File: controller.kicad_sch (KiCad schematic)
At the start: 40 parts, among them U1 TMC4671, U2 74LVC3G17, U3 74LVC3G17

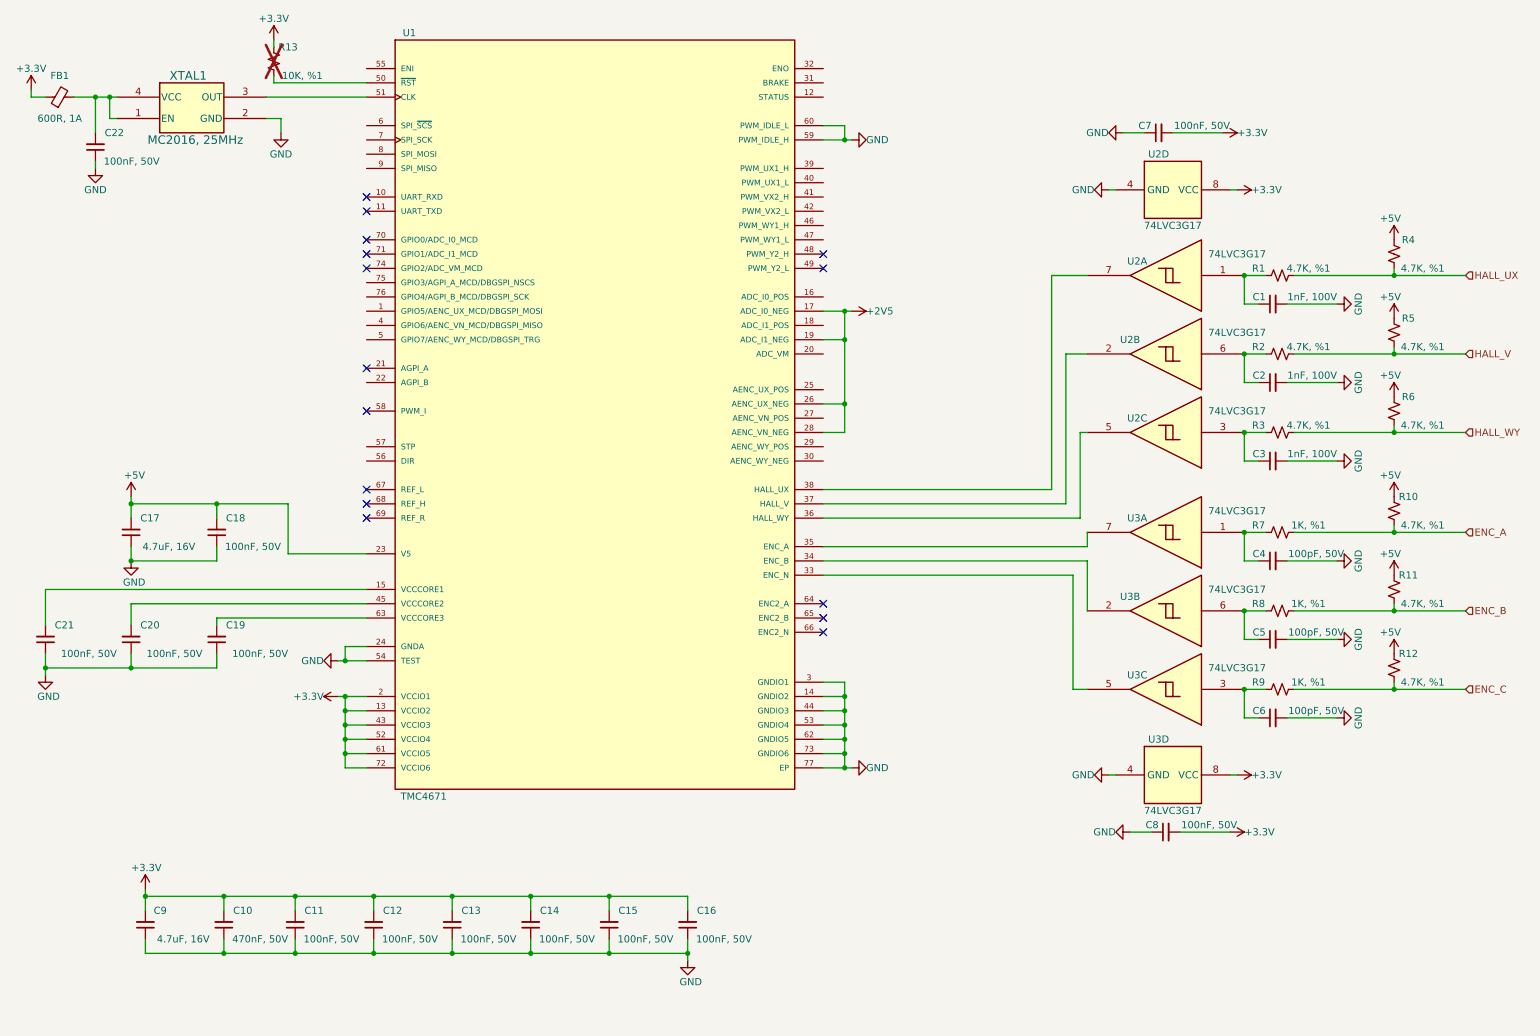
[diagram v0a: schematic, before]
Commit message: Finish controller and driver schematics.
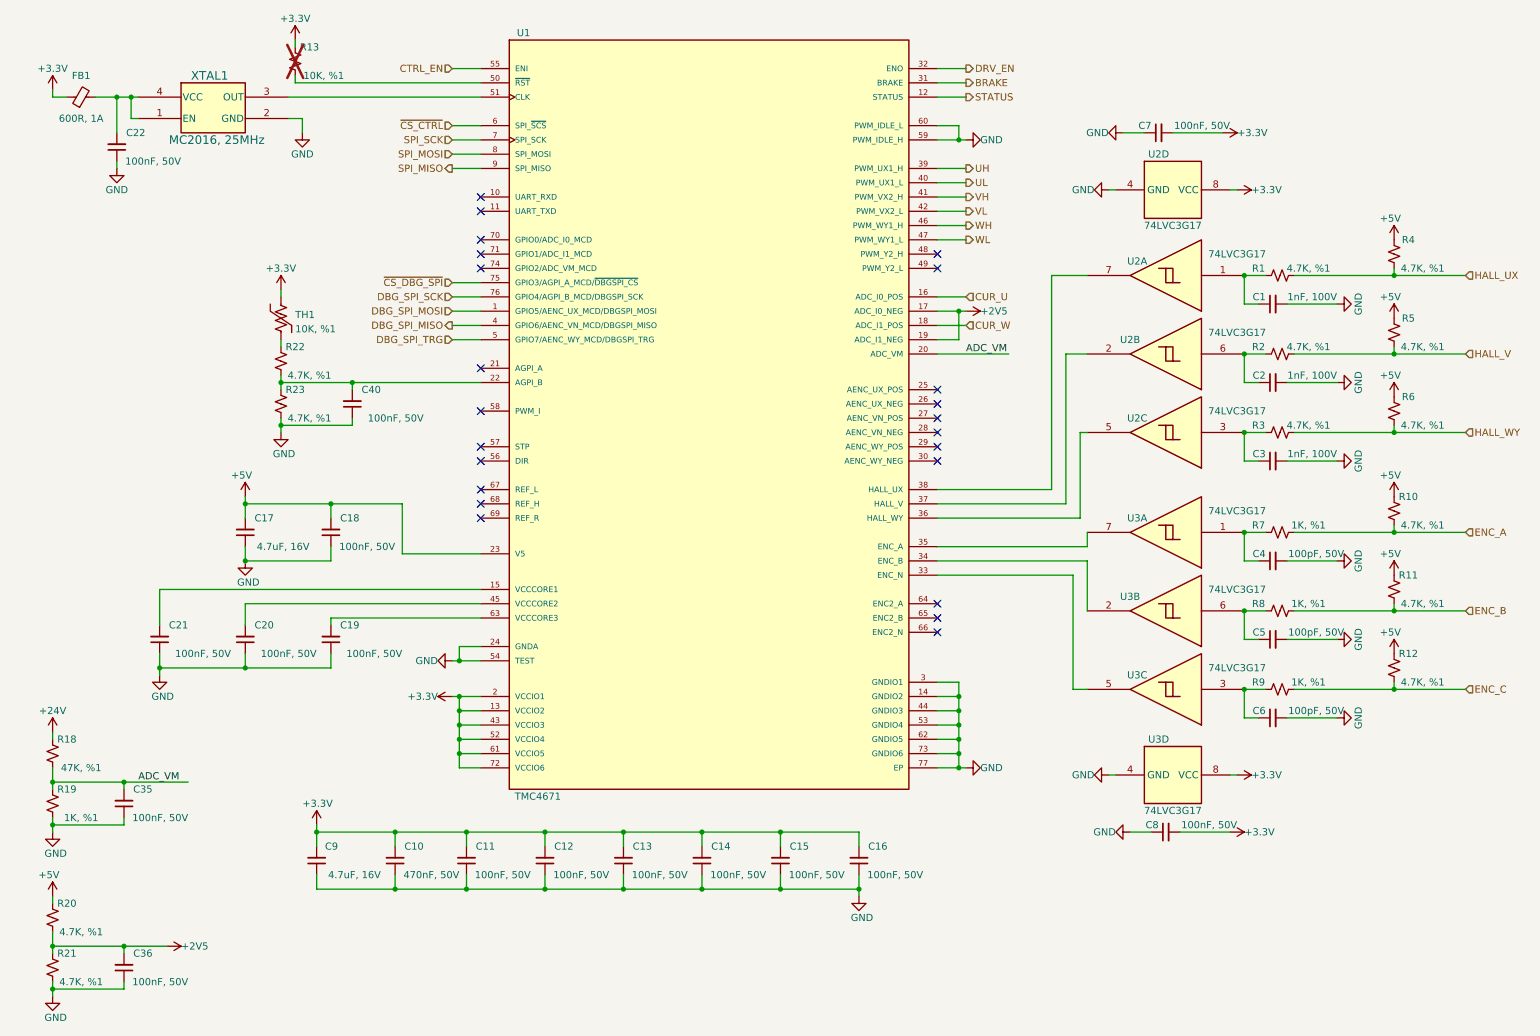
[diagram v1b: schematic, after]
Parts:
- added C35, C36, C40: 100nF, 50V, symbol Device:C_Small
- added R18: 47K, %1, symbol Device:R_Small_US
- added R19: 1K, %1, symbol Device:R_Small_US
- added R20, R21, R22, R23: 4.7K, %1, symbol Device:R_Small_US
- added TH1: 10K, %1, symbol Device:Thermistor_US
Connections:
- net +2V5: now also C36.2, R20.1, R21.2; no longer U1.26 (AENC_UX_NEG), U1.28 (AENC_VN_NEG)
- net +3.3V: now also TH1.1
- net +5V: now also R20.2
- net GND: now also C35.1, C36.1, C40.1, R19.1, R21.1, R23.1
- net DBG_SPI_MOSI: now reaches U1.1 (GPIO5/AENC_UX_MCD/DBGSPI_MOSI)
- net STATUS: now reaches U1.12 (STATUS)
- net CUR_U: now reaches U1.16 (ADC_I0_POS)
- net CUR_W: now reaches U1.18 (ADC_I1_POS)
- net ADC_VM: now reaches U1.20 (ADC_VM)
- net ADC_VM: now also C35.2, R18.1, R19.2
- net at U1.22 (AGPI_B): now also C40.2, R22.1, R23.2
- net BRAKE: now reaches U1.31 (BRAKE)
- net DRV_EN: now reaches U1.32 (ENO)
- net UH: now reaches U1.39 (PWM_UX1_H)
- net DBG_SPI_MISO: now reaches U1.4 (GPIO6/AENC_VN_MCD/DBGSPI_MISO)
- net UL: now reaches U1.40 (PWM_UX1_L)
- net VH: now reaches U1.41 (PWM_VX2_H)
- net VL: now reaches U1.42 (PWM_VX2_L)
- net WH: now reaches U1.46 (PWM_WY1_H)
- net WL: now reaches U1.47 (PWM_WY1_L)
- net DBG_SPI_TRG: now reaches U1.5 (GPIO7/AENC_WY_MCD/DBGSPI_TRG)
- net CTRL_EN: now reaches U1.55 (ENI)
- net ~{CS_CTRL}: now reaches U1.6 (SPI_~{SCS})
- net SPI_SCK: now reaches U1.7 (SPI_SCK)
- net ~{CS_DBG_SPI}: now reaches U1.75 (GPIO3/AGPI_A_MCD/~{DBGSPI_CS})
- net DBG_SPI_SCK: now reaches U1.76 (GPIO4/AGPI_B_MCD/DBGSPI_SCK)
- net SPI_MOSI: now reaches U1.8 (SPI_MOSI)
- net SPI_MISO: now reaches U1.9 (SPI_MISO)
- new net: R22.2, TH1.2
- new net +24V: R18.2
- no-connect marks 15 -> 23
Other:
- moved on the sheet: C10, C11, C12, C13, C14, C15, C16, C17, C18, C19, C20, C21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

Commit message: Assign footprints and part numbers.
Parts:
- C1, C2, C3: footprint (none) -> Capacitor_SMD:C_0603_1608Metric; MPN (none) -> C0603C102K1RAC7867
- C10: footprint (none) -> Capacitor_SMD:C_0603_1608Metric; MPN (none) -> C1608X7R1H474K080AC
- C11, C12, C13, C14, C15, C16, C18, C19, C20, C21, C22, C35, C36, C40, C7, C8: footprint (none) -> Capacitor_SMD:C_0603_1608Metric; MPN (none) -> C0603C103K5RAC7867
- C17, C9: footprint (none) -> Capacitor_SMD:C_0805_2012Metric; MPN (none) -> C0805C475K4RAC7800
- C4, C5, C6: footprint (none) -> Capacitor_SMD:C_0603_1608Metric; MPN (none) -> C0603C101K5RAC7867
- FB1: footprint (none) -> Resistor_SMD:R_0603_1608Metric
- R1, R10, R11, R12, R2, R20, R21, R22, R23, R3, R4, R5, R6: footprint (none) -> Resistor_SMD:R_0603_1608Metric; MPN (none) -> ERJ-3EKF4701V
- R13, TH1: footprint (none) -> Resistor_SMD:R_0603_1608Metric; MPN (none) -> NCP18XH103F03RB
- R18: footprint (none) -> Resistor_SMD:R_0603_1608Metric; MPN (none) -> ERJ-3EKF4702V
- R19, R7, R8, R9: footprint (none) -> Resistor_SMD:R_0603_1608Metric; MPN (none) -> ERJ-3EKF1001V
- U1: MPN (none) -> TMC4671-LA
- U2, U3: footprint (none) -> Package_SO:VSSOP-8_2.3x2mm_P0.5mm; MPN (none) -> 74LVC3G17DC,125

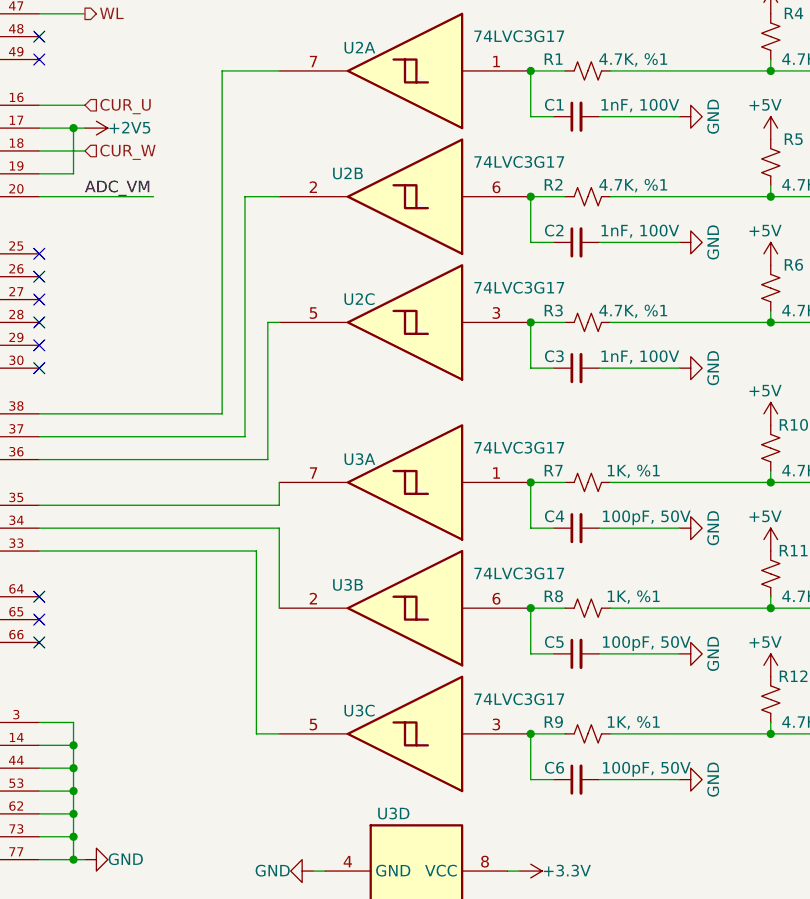
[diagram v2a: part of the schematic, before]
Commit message: Finish the initial placement, switch most of the parts to 0402.
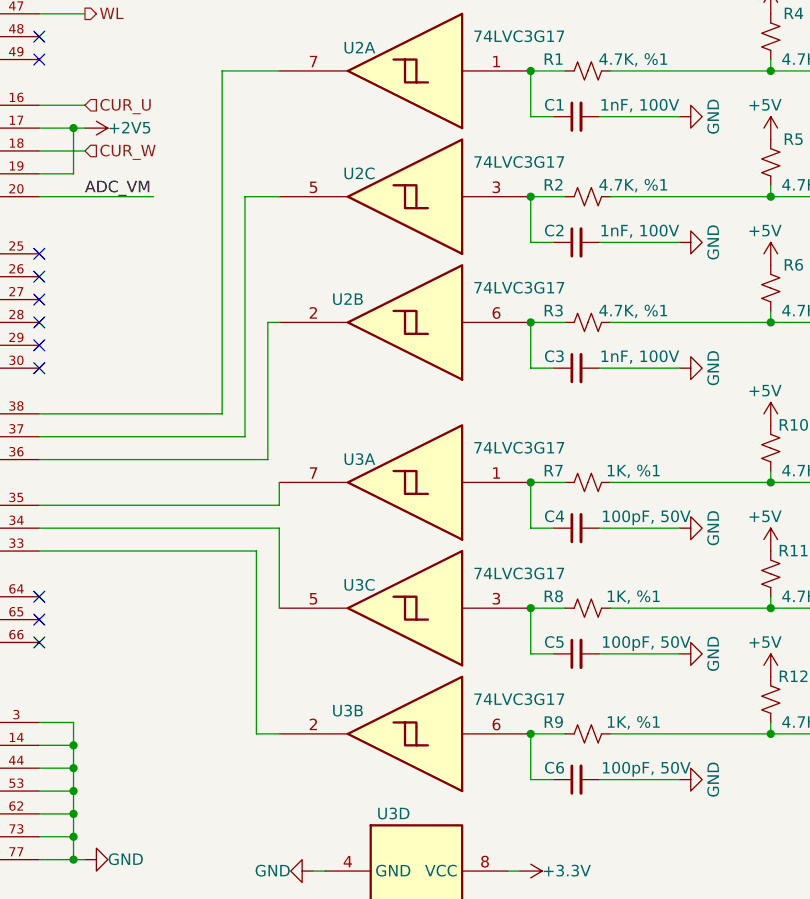
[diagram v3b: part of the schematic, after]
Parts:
- C1, C2, C3: footprint Capacitor_SMD:C_0603_1608Metric -> Capacitor_SMD:C_0402_1005Metric; MPN C0603C102K1RAC7867 -> 885012205080
- C11, C12, C13, C14, C15, C16, C18, C19, C20, C21, C22, C35, C36, C40, C7, C8: footprint Capacitor_SMD:C_0603_1608Metric -> Capacitor_SMD:C_0402_1005Metric; MPN C0603C103K5RAC7867 -> CL05B104KB54PNC
- C17, C9: footprint Capacitor_SMD:C_0805_2012Metric -> Capacitor_SMD:C_0603_1608Metric; MPN C0805C475K4RAC7800 -> GRM188Z71C475KE21J
- C4, C5, C6: footprint Capacitor_SMD:C_0603_1608Metric -> Capacitor_SMD:C_0402_1005Metric; MPN C0603C101K5RAC7867 -> 885012205055
- R1, R10, R11, R12, R2, R20, R21, R22, R23, R3, R4, R5, R6: footprint Resistor_SMD:R_0603_1608Metric -> Resistor_SMD:R_0402_1005Metric; MPN ERJ-3EKF4701V -> ERJ-2RKF4701X
- R13: footprint Resistor_SMD:R_0603_1608Metric -> Resistor_SMD:R_0402_1005Metric; MPN NCP18XH103F03RB -> RC1005F103CS
- R18: footprint Resistor_SMD:R_0603_1608Metric -> Resistor_SMD:R_0402_1005Metric; MPN ERJ-3EKF4702V -> ERJ-2RKF4702X
- R19, R7, R8, R9: footprint Resistor_SMD:R_0603_1608Metric -> Resistor_SMD:R_0402_1005Metric; MPN ERJ-3EKF1001V -> ERJ-2RKF1001X
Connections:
- net at C2.1, R2.1: now also U2.3; no longer U2.6
- net at C5.1, R8.1: now also U3.3; no longer U3.6
- net at U1.33 (ENC_N): now also U3.2; no longer U3.5
- net at U1.34 (ENC_B): now also U3.5; no longer U3.2
- net at U1.36 (HALL_WY): now also U2.2; no longer U2.5
- net at U1.37 (HALL_V): now also U2.5; no longer U2.2
- net at C6.1, R9.1: now also U3.6; no longer U3.3
- net at C3.1, R3.1: now also U2.6; no longer U2.3

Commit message: Cleanup part properties.
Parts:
- U1: MANUFACTURER Trinamic Motion -> (none); MAXIMUM_PACKAGE_HEIGHT 0.9mm -> (none); PARTREV V1.06 -> (none); STANDARD IPC 7351B -> (none)
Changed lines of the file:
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@@
       (effects (font (size 1.27 1.27)) hide)
-    )
-    (property "MAXIMUM_PACKAGE_HEIGHT" "0.9mm" (at 137.16 92.71 0)
-      (effects (font (size 1.27 1.27)) (justify bottom) hide)
-    )
-    (property "MANUFACTURER" "Trinamic Motion" (at 137.16 92.71 0)
-      (effects (font (size 1.27 1.27)) (justify bottom) hide)
-    )
-    (property "PARTREV" "V1.06" (at 137.16 92.71 0)
-      (effects (font (size 1.27 1.27)) (justify bottom) hide)
-    )
-    (property "STANDARD" "IPC 7351B" (at 137.16 92.71 0)
-      (effects (font (size 1.27 1.27)) (justify bottom) hide)
     )
     (property "MPN" "TMC4671-LA" (at 137.16 92.71 0)

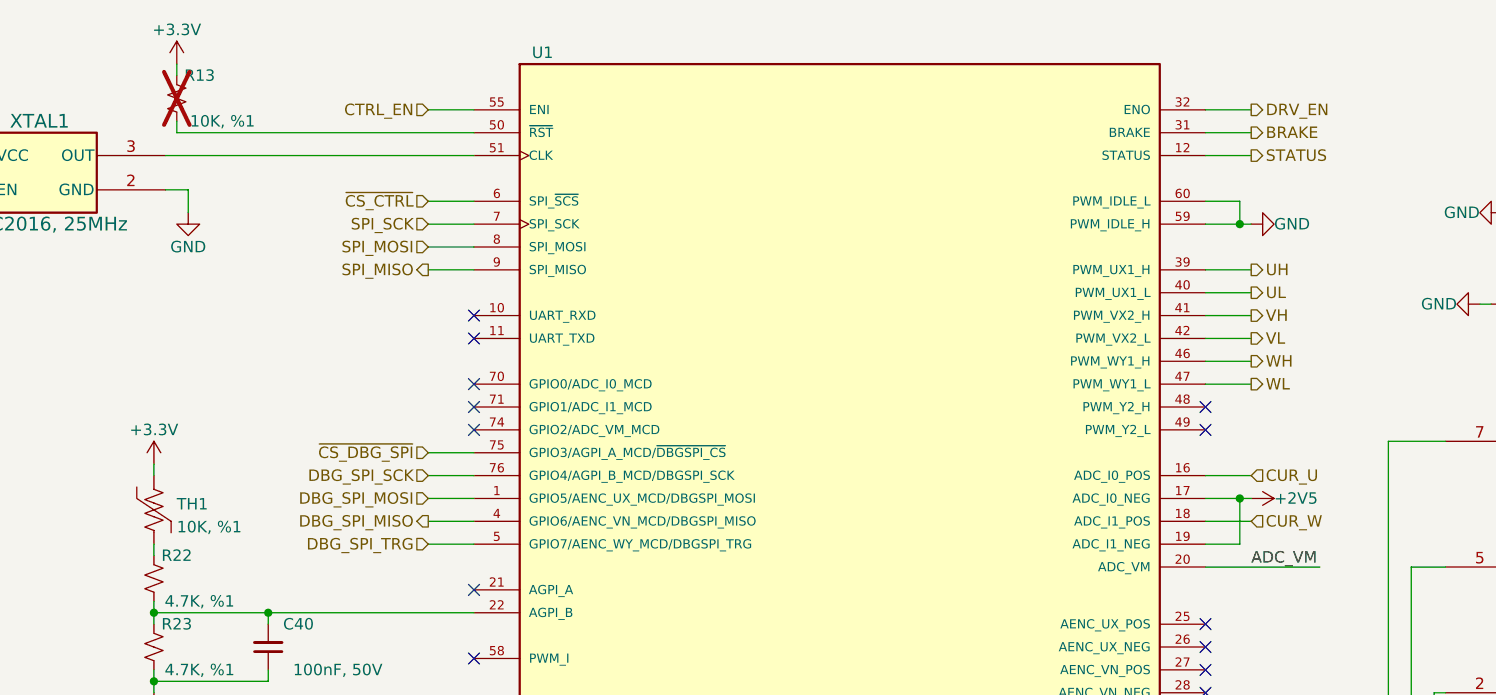
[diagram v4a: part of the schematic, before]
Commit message: Fix issues found during the test, in the schematics.
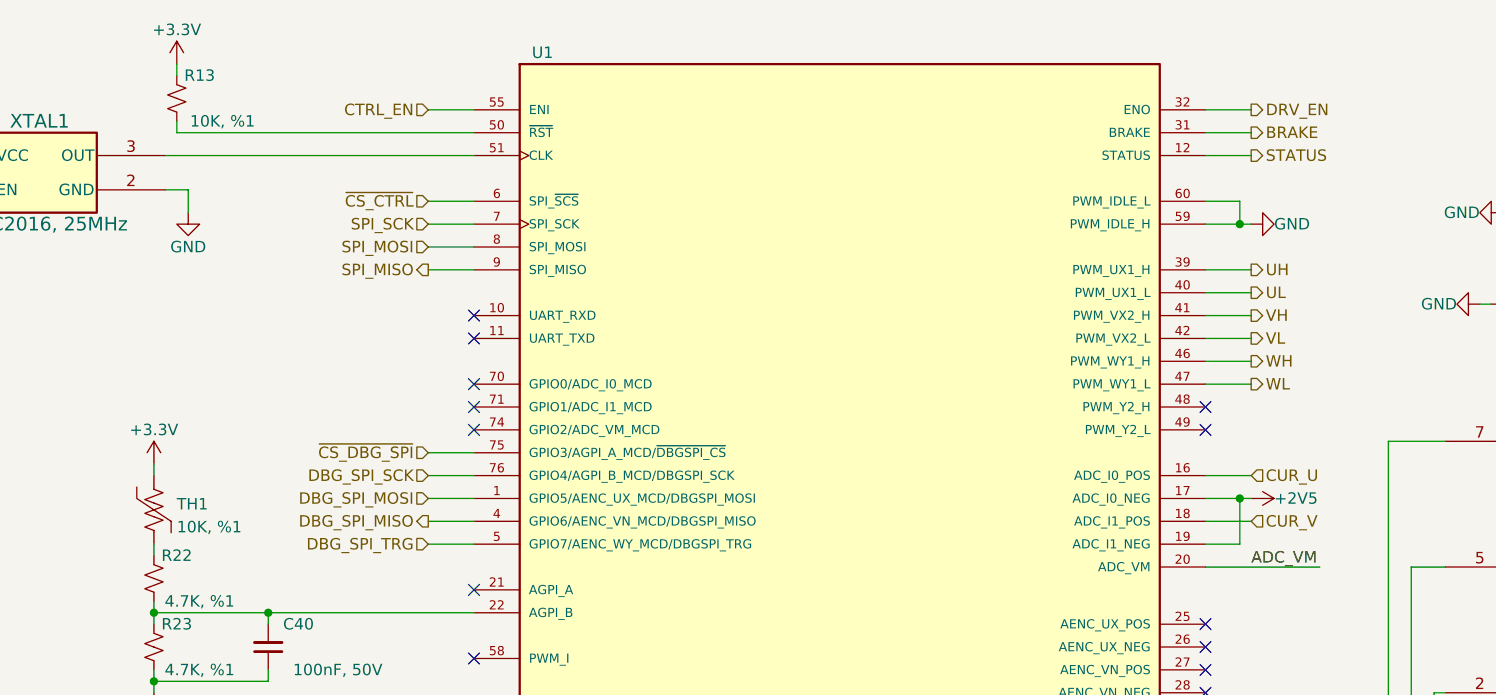
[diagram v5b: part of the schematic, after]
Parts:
- R13: now fitted
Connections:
- net CUR_W renamed CUR_V
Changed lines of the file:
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@@
     (effects (font (size 1.27 1.27)) (justify left))
   )
-  (hierarchical_label "CUR_W" (shape input) (at 182.88 72.39 0) (fields_autoplaced)
+  (hierarchical_label "CUR_V" (shape input) (at 182.88 72.39 0) (fields_autoplaced)
     (effects (font (size 1.27 1.27)) (justify left))
   )
@@
   )
   (symbol (lib_id "Device:R_Small_US") (at 63.5 25.4 180) (unit 1)
-    (in_bom yes) (on_board yes) (dnp yes)
+    (in_bom yes) (on_board yes) (dnp no)
     (property "Reference" "R13" (at 66.04 22.86 0)
       (effects (font (size 1.27 1.27)))
